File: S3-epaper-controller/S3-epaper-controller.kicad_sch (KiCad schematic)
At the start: 65 parts, among them P1 CONN_02X13, U1 ESP32-S3-DEVKITC-1-N8R2, U3 QFN50P700X700X100-49N, U6 ED060XC5

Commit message: Add S3 devkit board prototype
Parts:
- U1: footprint XCVR_ESP32-S3-DEVKITC-1-N8R2 -> ESP32S3:ESP32-S3-DEVKITC-1-N8R2
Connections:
- net GND: no longer P1.20 (Pin_20)
- net SCL: now also P1.16 (Pin_16); no longer P1.14 (Pin_14)
- net SDA: now also P1.14 (Pin_14); no longer P1.16 (Pin_16)
- net SW_VIN: no longer P1.25 (Pin_25)
- net TPS_PWR_GOOD: no longer P1.18 (Pin_18)
- net TPS_nINT: now also U1.J1_17 (GPIO11)
- no-connect marks 25 -> 28
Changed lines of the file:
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@@
   (no_connect (at 184.15 166.37))
   (no_connect (at 176.53 166.37))
+  (no_connect (at 179.07 151.13))
   (no_connect (at 196.85 95.25))
   (no_connect (at 196.85 100.33))
   (no_connect (at 173.99 166.37))
   (no_connect (at 179.07 166.37))
+  (no_connect (at 181.61 153.67))
   (no_connect (at 265.43 109.22))
   (no_connect (at 316.23 88.9))
@@
   (no_connect (at 196.85 90.17))
   (no_connect (at 166.37 166.37))
+  (no_connect (at 189.23 166.37))
   (no_connect (at 265.43 86.36))
   (no_connect (at 196.85 102.87))
@@
     (stroke (width 0) (type default) (color 0 0 0 0))
   )
-  (wire (pts (xy 189.23 167.64) (xy 189.23 166.37))
-    (stroke (width 0) (type default) (color 0 0 0 0))
-  )
   (wire (pts (xy 262.89 119.38) (xy 262.89 120.65))
     (stroke (width 0) (type default) (color 0 0 0 0))
@@
     (stroke (width 0) (type default) (color 0 0 0 0))
   )
-  (wire (pts (xy 181.61 153.67) (xy 181.61 143.51))
-    (stroke (width 0) (type default) (color 0 0 0 0))
-  )
   (wire (pts (xy 336.55 109.22) (xy 336.55 106.68))
     (stroke (width 0) (type default) (color 0 0 0 0))
@@
     (stroke (width 0) (type default) (color 0 0 0 0))
   )
-  (wire (pts (xy 181.61 143.51) (xy 182.88 143.51))
-    (stroke (width 0) (type default) (color 0 0 0 0))
-  )
   (wire (pts (xy 257.81 53.34) (xy 257.81 52.07))
     (stroke (width 0) (type default) (color 0 0 0 0))
@@
     (effects (font (size 1.27 1.27)) (justify left bottom))
   )
-  (label "SDA" (at 176.53 151.13 90)
-    (effects (font (size 1.27 1.27)) (justify left bottom))
-  )
   (label "VNEG_IN" (at 250.19 114.3 0)
     (effects (font (size 1.27 1.27)) (justify left bottom))
@@
     (effects (font (size 1.27 1.27)) (justify left bottom))
   )
-  (label "SCL" (at 173.99 151.13 90)
-    (effects (font (size 1.27 1.27)) (justify left bottom))
-  )
   (label "EP_D7" (at 151.13 90.17 180)
     (effects (font (size 1.27 1.27)) (justify right bottom))
@@
     (effects (font (size 1.27 1.27)) (justify left bottom))
   )
-  (label "+5V" (at 189.23 167.64 270)
-    (effects (font (size 1.27 1.27)) (justify right bottom))
-  )
   (label "-20V" (at 99.06 142.24 180)
     (effects (font (size 1.27 1.27)) (justify right bottom))
@@
     (effects (font (size 1.27 1.27)) (justify right bottom))
   )
-  (label "TPS_nINT" (at 147.32 100.33 180)
+  (label "TPS_nINT" (at 151.13 100.33 180)
     (effects (font (size 1.27 1.27)) (justify right bottom))
   )
@@
     (effects (font (size 1.27 1.27)) (justify left bottom))
   )
+  (label "SCL" (at 176.53 151.13 90)
+    (effects (font (size 1.27 1.27)) (justify left bottom))
+  )
   (label "EP_CKV" (at 59.69 110.49 0)
     (effects (font (size 1.27 1.27)) (justify left bottom))
@@
     (effects (font (size 1.27 1.27)) (justify left bottom))
   )
-  (label "TPS_PWR_GOOD" (at 179.07 151.13 90)
+  (label "SDA" (at 173.99 151.13 90)
     (effects (font (size 1.27 1.27)) (justify left bottom))
   )
@@
     (pin "2")
   )
-  (symbol (lib_id "power:GND") (at 182.88 143.51 0) (unit 1)
-    (in_bom yes) (on_board yes) (fields_autoplaced)
-    (property "Reference" "#PWR01" (id 0) (at 182.88 149.86 0)
-      (effects (font (size 1.27 1.27)) hide)
-    )
-    (property "Value" "GND" (id 1) (at 182.88 148.0725 0))
-    (property "Footprint" "" (id 2) (at 182.88 143.51 0)
-      (effects (font (size 1.27 1.27)) hide)
-    )
-    (property "Datasheet" "" (id 3) (at 182.88 143.51 0)
-      (effects (font (size 1.27 1.27)) hide)
-    )
-    (pin "1")
-  )
   (symbol (lib_id "Device:R") (at 215.9 81.28 180) (unit 1)
     (in_bom yes) (on_board yes) (fields_autoplaced)
@@
     (property "Reference" "U1" (id 0) (at 173.99 55.9902 0))
     (property "Value" "ESP32-S3-DEVKITC-1-N8R2" (id 1) (at 173.99 58.5271 0))
-    (property "Footprint" "XCVR_ESP32-S3-DEVKITC-1-N8R2" (id 2) (at 173.99 92.71 0)
+    (property "Footprint" "ESP32S3:ESP32-S3-DEVKITC-1-N8R2" (id 2) (at 173.99 92.71 0)
       (effects (font (size 1.27 1.27)) (justify left bottom) hide)
     )
@@
       (reference "#FLG0107") (unit 1) (value "PWR_FLAG") (footprint "")
     )
-    (path "/72cb2d99-82ac-4459-9b03-9d37c2c785bc"
-      (reference "#PWR01") (unit 1) (value "GND") (footprint "")
-    )
     (path "/00000000-0000-0000-0000-00006edbd861"
       (reference "#PWR02") (unit 1) (value "GND") (footprint "")
@@
     )
     (path "/d21c872f-2158-437c-a347-1cca2ba28d91"
-      (reference "U1") (unit 1) (value "ESP32-S3-DEVKITC-1-N8R2") (footprint "XCVR_ESP32-S3-DEVKITC-1-N8R2")
+      (reference "U1") (unit 1) (value "ESP32-S3-DEVKITC-1-N8R2") (footprint "ESP32S3:ESP32-S3-DEVKITC-1-N8R2")
     )
     (path "/00000000-0000-0000-0000-0000607396d1"

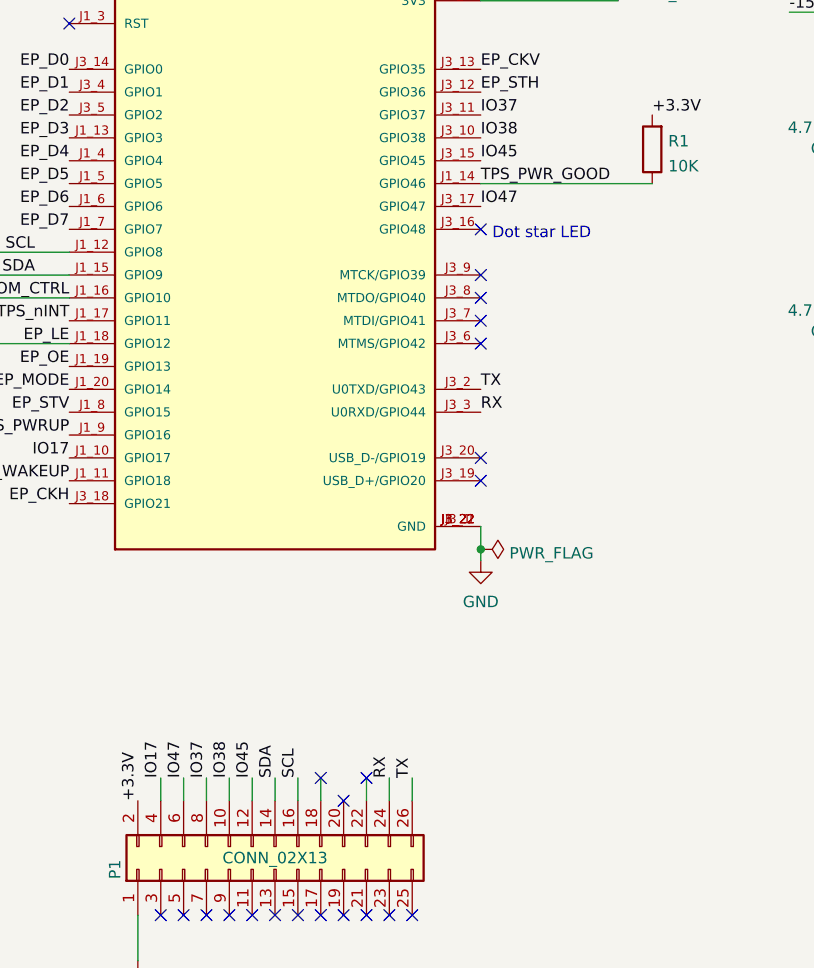
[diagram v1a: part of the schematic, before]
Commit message: REF https://github.com/martinberlin/epdiy-rotation/issues/6 Do not use IO46 (strapping pin)
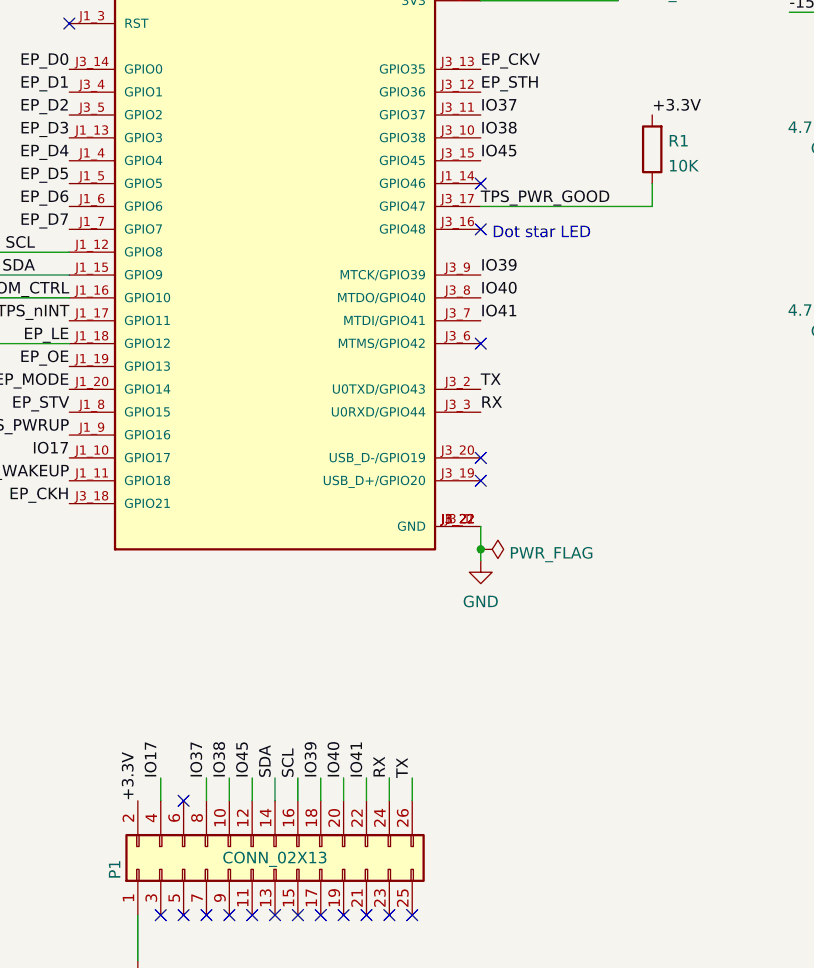
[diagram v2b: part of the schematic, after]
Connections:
- net TPS_PWR_GOOD: now also U1.J3_17 (GPIO47); no longer U1.J1_14 (GPIO46)
- net IO39: now reaches P1.18 (Pin_18)
- net IO39: now also U1.J3_9 (MTCK/GPIO39)
- net IO40: now reaches P1.20 (Pin_20)
- net IO40: now also U1.J3_8 (MTDO/GPIO40)
- net IO41: now reaches P1.22 (Pin_22)
- net IO41: now also U1.J3_7 (MTDI/GPIO41)
- net IO47: no longer names the net of P1.6 (Pin_6)
- net IO47: no longer U1.J3_17 (GPIO47)
- no-connect marks 28 -> 24

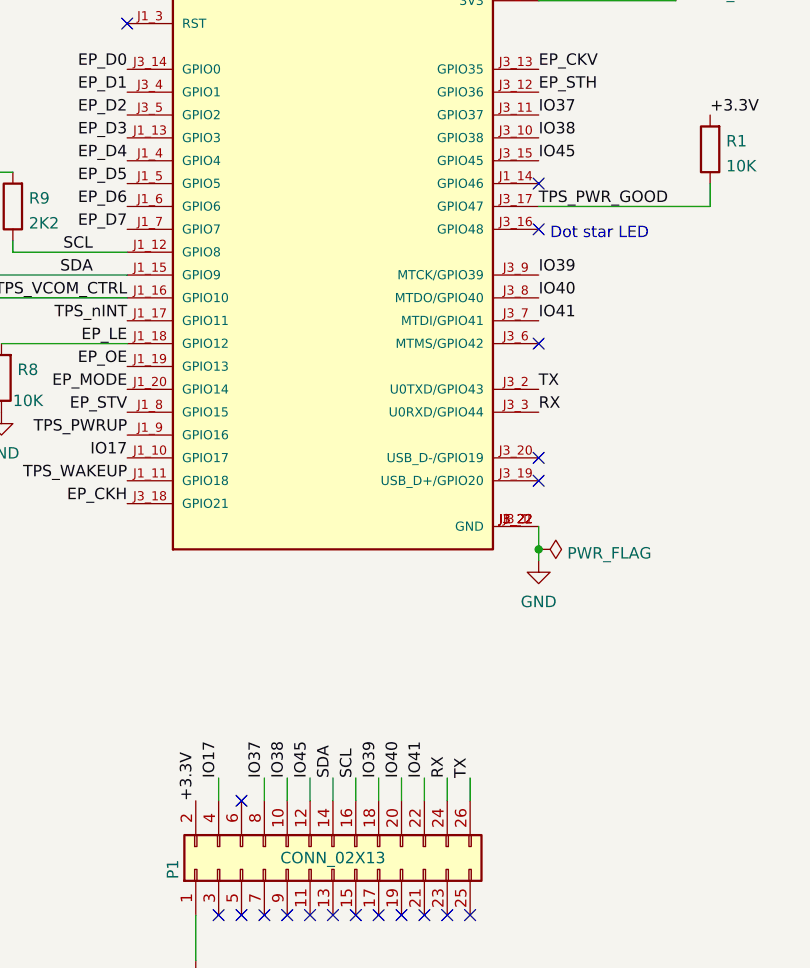
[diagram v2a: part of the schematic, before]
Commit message: Update some IOs + documentation
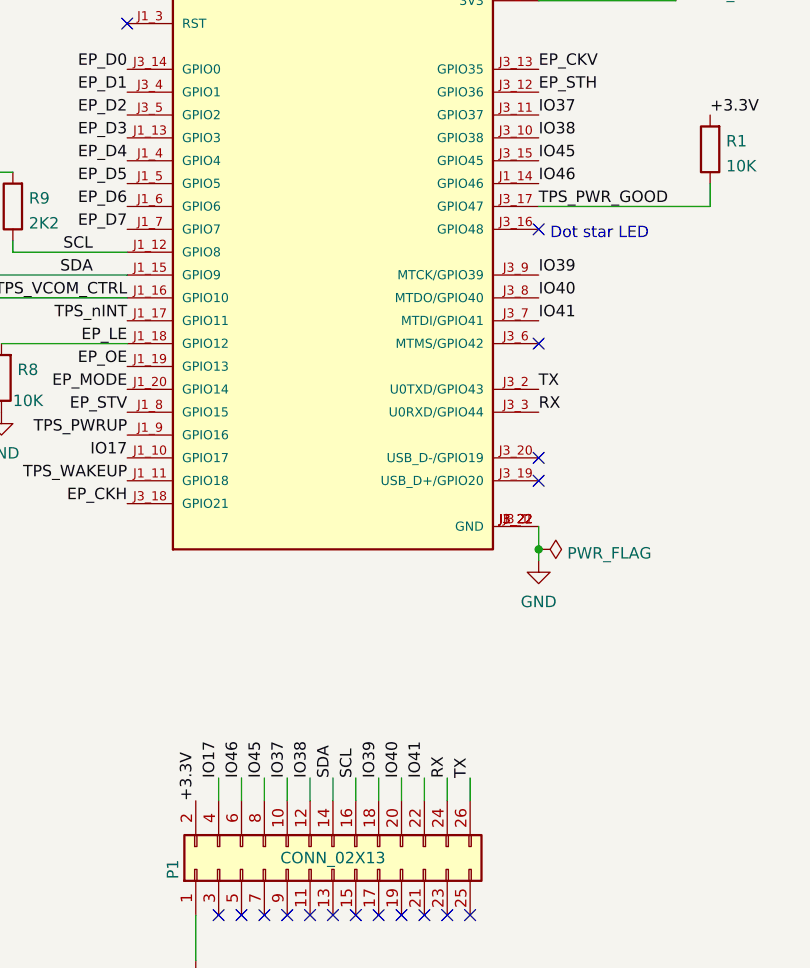
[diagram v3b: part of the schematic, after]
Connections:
- net IO37: now also P1.10 (Pin_10); no longer P1.8 (Pin_8)
- net IO38: now also P1.12 (Pin_12); no longer P1.10 (Pin_10)
- net IO45: now also P1.8 (Pin_8); no longer P1.12 (Pin_12)
- net IO46: now reaches P1.6 (Pin_6)
- net IO46: now also U1.J1_14 (GPIO46)
- no-connect marks 24 -> 22
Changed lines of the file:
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@@
   (no_connect (at 196.85 118.11))
   (no_connect (at 184.15 166.37))
-  (no_connect (at 196.85 85.09))
   (no_connect (at 176.53 166.37))
   (no_connect (at 173.99 166.37))
   (no_connect (at 179.07 166.37))
-  (no_connect (at 163.83 153.67))
   (no_connect (at 265.43 109.22))
   (no_connect (at 316.23 88.9))
@@
     (stroke (width 0) (type default) (color 0 0 0 0))
   )
+  (wire (pts (xy 163.83 151.13) (xy 163.83 153.67))
+    (stroke (width 0) (type default) (color 0 0 0 0))
+  )
   (wire (pts (xy 68.58 110.49) (xy 59.69 110.49))
     (stroke (width 0) (type default) (color 0 0 0 0))
@@
     (effects (font (size 1.27 1.27)) (justify left bottom))
   )
+  (label "IO38" (at 171.45 151.13 90)
+    (effects (font (size 1.27 1.27)) (justify left bottom))
+  )
   (label "VNEG_IN" (at 250.19 114.3 0)
     (effects (font (size 1.27 1.27)) (justify left bottom))
@@
     (effects (font (size 1.27 1.27)) (justify left bottom))
   )
+  (label "IO46" (at 163.83 151.13 90)
+    (effects (font (size 1.27 1.27)) (justify left bottom))
+  )
   (label "EP_D2" (at 151.13 77.47 180)
     (effects (font (size 1.27 1.27)) (justify right bottom))
@@
     (effects (font (size 1.27 1.27)) (justify left bottom))
   )
+  (label "IO46" (at 196.85 85.09 0)
+    (effects (font (size 1.27 1.27)) (justify left bottom))
+  )
   (label "EP_D6" (at 151.13 87.63 180)
     (effects (font (size 1.27 1.27)) (justify right bottom))
@@
     (effects (font (size 1.27 1.27)) (justify left bottom))
   )
-  (label "IO45" (at 171.45 151.13 90)
-    (effects (font (size 1.27 1.27)) (justify left bottom))
-  )
   (label "15V" (at 368.3 64.77 180)
     (effects (font (size 1.27 1.27)) (justify right bottom))
@@
     (effects (font (size 1.27 1.27)) (justify left bottom))
   )
-  (label "IO38" (at 168.91 151.13 90)
-    (effects (font (size 1.27 1.27)) (justify left bottom))
-  )
   (label "15V" (at 259.08 106.68 0)
     (effects (font (size 1.27 1.27)) (justify left bottom))
@@
     (effects (font (size 1.27 1.27)) (justify left bottom))
   )
+  (label "IO45" (at 166.37 151.13 90)
+    (effects (font (size 1.27 1.27)) (justify left bottom))
+  )
   (label "+5V" (at 199.39 62.23 0)
     (effects (font (size 1.27 1.27)) (justify left bottom))
   )
+  (label "IO37" (at 168.91 151.13 90)
+    (effects (font (size 1.27 1.27)) (justify left bottom))
+  )
   (label "TPS_PWR_GOOD" (at 196.85 87.63 0)
     (effects (font (size 1.27 1.27)) (justify left bottom))
@@
     (effects (font (size 1.27 1.27)) (justify right bottom))
   )
-  (label "IO37" (at 166.37 151.13 90)
-    (effects (font (size 1.27 1.27)) (justify left bottom))
-  )
   (label "TPS_WAKEUP" (at 151.13 118.11 180)
